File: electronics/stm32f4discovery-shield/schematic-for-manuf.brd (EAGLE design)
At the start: 101.6 x 105.4 mm, 43 parts, among them IC1 MAX3468CPA, IC3 LM340H-12, IC4 LM340H-12, J1 POWER_JACKSLT, Q1 BC548

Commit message: Algumas alteracoes, adicao de anotacoes.
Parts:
- moved I2C3_IMU 5.43 mm to (90.8, 82.7)
- moved AN1 1.27 mm to (10.5, 74.3)
- moved US2 1.27 mm to (10.5, 57.5)
- moved I2C1_ESC 0.64 mm to (90.8, 60.0)
- moved SPI1 0.64 mm to (90.8, 42.9)
- moved US6 0.63 mm to (9.84, 14.9)
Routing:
- net 5V: track 431.6 -> 425.5 mm
- net N$9: track 53.4 -> 48.3 mm
- net SDA2: track 91.1 -> 87.5 mm
- net GND: track 17.8 -> 14.4 mm
- net 3.3V: track 134.9 -> 136.2 mm
- net PA3/USART2_RX: track 28.5 -> 27.2 mm
- net PA2/USART2_TX: track 16.5 -> 17.7 mm
- net N$10: track 8.29 -> 9.49 mm
- net ADC3: track 27.6 -> 26.4 mm
- net ADC1: track 17.6 -> 18.6 mm
- net PB3/SPI1_SCK: track 24.4 -> 23.7 mm
- net SCL1: track 50.1 -> 49.4 mm
- net PC6/USART6_TX: track 68.7 -> 69.3 mm
- net SDA1: track 67.8 -> 68.4 mm
- net PB4/SPI1_MISO: track 23.1 -> 23.7 mm
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
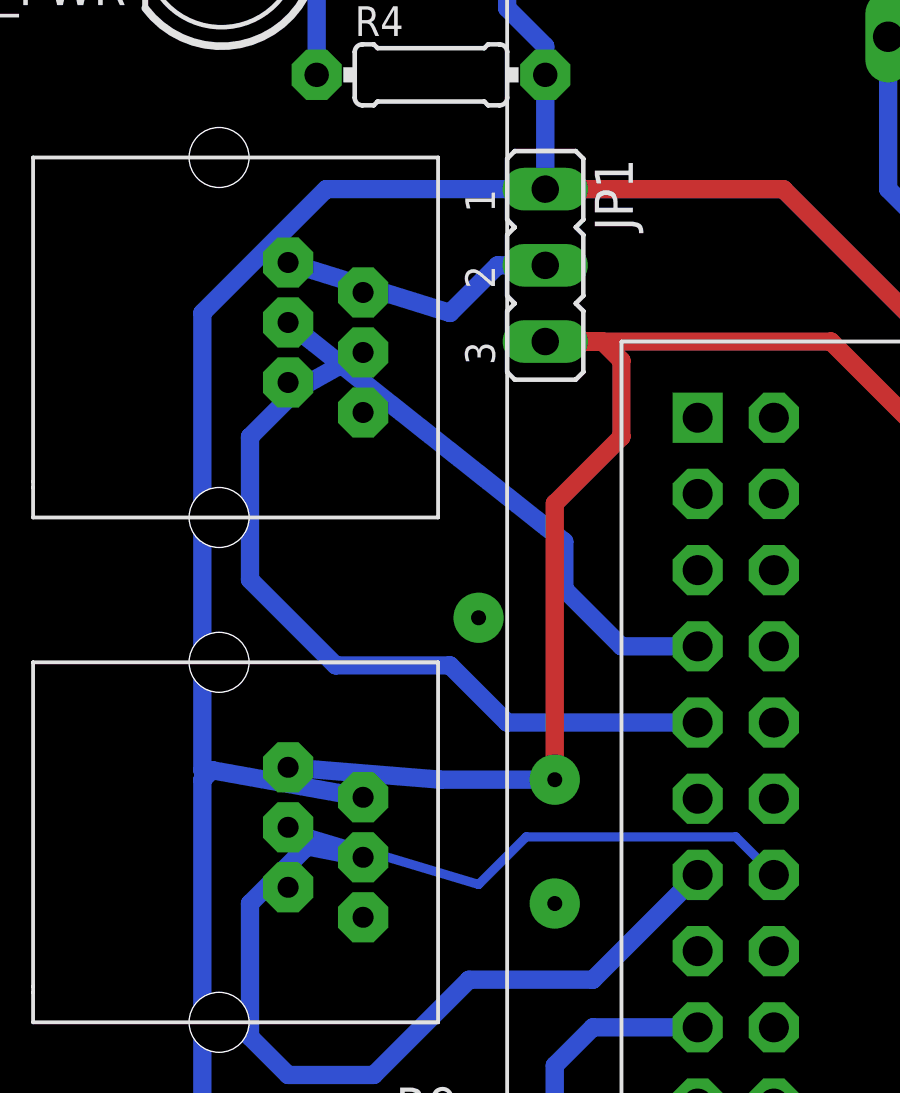
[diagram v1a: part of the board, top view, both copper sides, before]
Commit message: new file:   .gitignore 	modified:   electronics/stm32f4discovery-shield/anotacoes_para_manufatura.txt 	modified:   electronics/stm32f4discovery-shield/schematic-for-manuf.brd
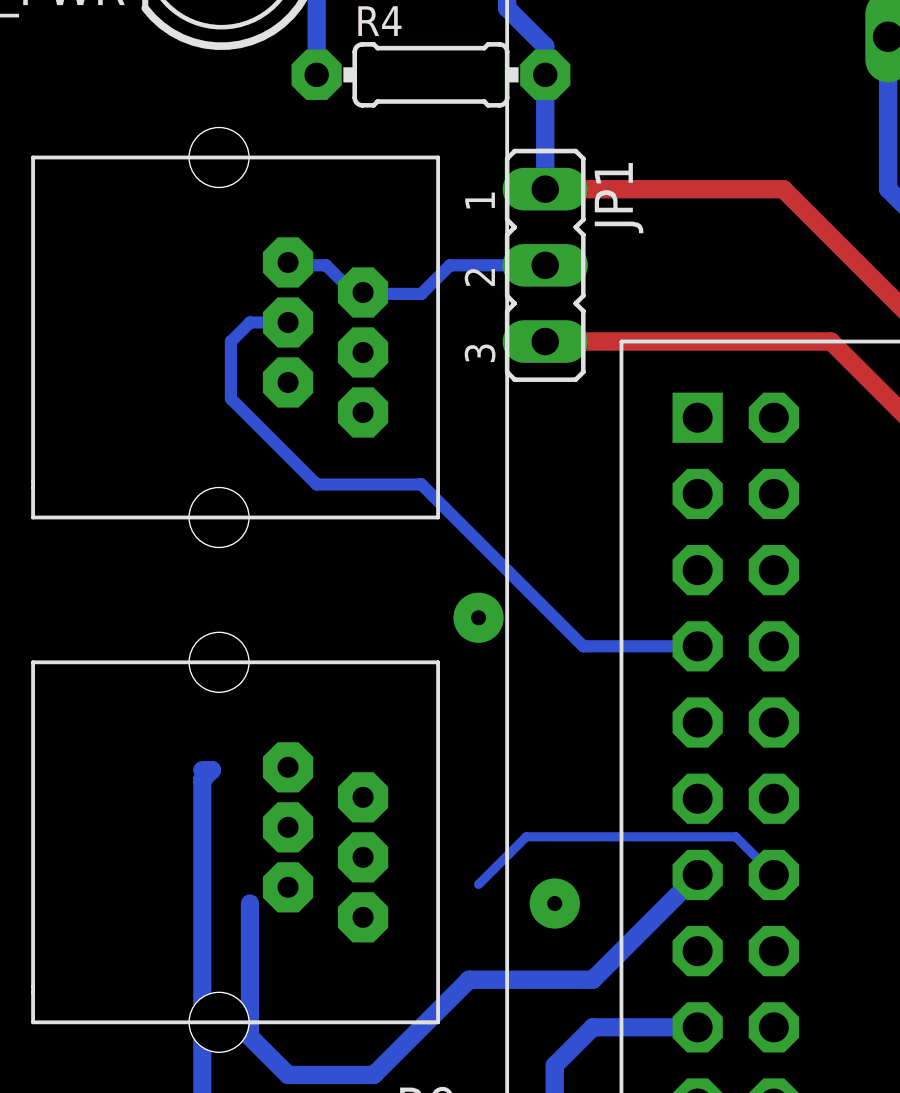
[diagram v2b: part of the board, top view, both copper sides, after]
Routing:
- net 5V: track 425.5 -> 392.0 mm
- net 3.3V: track 136.2 -> 109.2 mm, vias 1 -> 0
- net ADC3: track 26.4 -> 0.00 mm
- net PA2/USART2_TX: track 17.7 -> 11.0 mm
- net PA3/USART2_RX: track 27.2 -> 22.7 mm
- net ADC1: track 18.6 -> 23.0 mm
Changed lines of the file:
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@@
 <?xml version="1.0" encoding="utf-8"?>
 <!DOCTYPE eagle SYSTEM "eagle.dtd">
-<eagle version="6.4">
+<eagle version="6.5.0">
 <drawing>
 <settings>
@@
 <setting verticaltext="up"/>
 </settings>
-<grid distance="25" unitdist="mil" unit="mil" style="lines" multiple="1" display="yes" altdistance="0.025" altunitdist="inch" altunit="inch"/>
+<grid distance="12.5" unitdist="mil" unit="mil" style="lines" multiple="1" display="yes" altdistance="0.025" altunitdist="inch" altunit="inch"/>
 <layers>
 <layer number="1" name="Top" color="4" fill="1" visible="yes" active="yes"/>
@@
 </class>
 </classes>
-<designrules name="default">
+<designrules name="default *">
 <description language="de">&lt;b&gt;EAGLE Design Rules&lt;/b&gt;
 &lt;p&gt;
@@
 <param name="mdSmdStop" value="0mil"/>
 <param name="msWidth" value="10mil"/>
-<param name="msDrill" value="24mil"/>
+<param name="msDrill" value="0.4mm"/>
 <param name="msMicroVia" value="9.99mm"/>
 <param name="msBlindViaRatio" value="0.5"/>
@@
 <wire x1="89.535" y1="56.1975" x2="92.075" y2="56.1975" width="0.6096" layer="16"/>
 <wire x1="88.305" y1="59.0075" x2="89.535" y2="56.1975" width="0.6096" layer="16"/>
-<wire x1="7.62" y1="59.3725" x2="7.62" y2="74.6125" width="0.6096" layer="16"/>
 <wire x1="92.075" y1="56.1975" x2="92.075" y2="51.1175" width="0.6096" layer="16"/>
 <wire x1="92.075" y1="51.1175" x2="92.075" y2="50.8" width="0.6096" layer="16"/>
@@
 <wire x1="94.615" y1="58.7375" x2="92.075" y2="56.1975" width="0.6096" layer="16"/>
 <contactref element="JP1" pad="1"/>
-<wire x1="19.05" y1="78.74" x2="11.7475" y2="78.74" width="0.6096" layer="16"/>
-<wire x1="11.7475" y1="78.74" x2="7.62" y2="74.6125" width="0.6096" layer="16"/>
 <wire x1="17.78" y1="84.7725" x2="19.05" y2="83.5025" width="0.6096" layer="16"/>
 <wire x1="19.05" y1="83.5025" x2="19.05" y2="82.55" width="0.6096" layer="16"/>
@@
 <wire x1="95.5675" y1="13.6525" x2="93.0275" y2="11.1125" width="0.6096" layer="16"/>
 <wire x1="93.0275" y1="11.1125" x2="87.67" y2="13.9225" width="0.6096" layer="16"/>
-<wire x1="12.9775" y1="58.4675" x2="7.9375" y2="59.3725" width="0.6096" layer="16"/>
 <wire x1="7.9375" y1="59.3725" x2="7.62" y2="59.3725" width="0.6096" layer="16"/>
 <wire x1="88.305" y1="81.725" x2="93.345" y2="80.3275" width="0.6096" layer="16"/>
@@
 <wire x1="12.3425" y1="15.9225" x2="13.335" y2="17.4625" width="0.6096" layer="16"/>
 <wire x1="13.335" y1="17.4625" x2="9.8425" y2="16.9225" width="0.6096" layer="16"/>
+<wire x1="12.9775" y1="58.4675" x2="19.05" y2="78.74" width="0" layer="19" extent="16-16"/>
+<wire x1="7.9375" y1="59.3725" x2="12.9775" y2="58.4675" width="0" layer="19" extent="16-16"/>
 </signal>
 <signal name="3.3V">
@@
 <contactref element="JP1" pad="3"/>
 <wire x1="52.3875" y1="58.42" x2="49.8475" y2="60.96" width="0.6096" layer="16"/>
-<wire x1="19.05" y1="73.66" x2="20.955" y2="73.66" width="0.6096" layer="1"/>
-<wire x1="20.955" y1="73.66" x2="21.59" y2="73.025" width="0.6096" layer="1"/>
-<wire x1="21.59" y1="73.025" x2="21.59" y2="70.485" width="0.6096" layer="1"/>
-<wire x1="21.59" y1="70.485" x2="19.3675" y2="68.2625" width="0.6096" layer="1"/>
-<wire x1="19.3675" y1="68.2625" x2="19.3675" y2="59.055" width="0.6096" layer="1"/>
-<via x="19.3675" y="59.055" extent="1-16" drill="0.5" diameter="1.6764" shape="octagon"/>
-<wire x1="19.05" y1="59.3725" x2="19.3675" y2="59.055" width="0.6096" layer="16"/>
-<wire x1="10.4775" y1="59.4675" x2="15.5575" y2="59.055" width="0.6096" layer="16"/>
-<wire x1="15.5575" y1="59.055" x2="19.3675" y2="59.055" width="0.6096" layer="16"/>
 <wire x1="52.3875" y1="58.42" x2="53.975" y2="58.42" width="0.6096" layer="16"/>
 <wire x1="53.975" y1="58.42" x2="69.5325" y2="58.42" width="0.6096" layer="16"/>
@@
 <wire x1="49.8475" y1="67.6275" x2="49.8475" y2="64.77" width="0.6096" layer="16"/>
 <wire x1="49.8475" y1="64.77" x2="49.8475" y2="60.96" width="0.6096" layer="16"/>
+<wire x1="10.4775" y1="59.4675" x2="19.05" y2="73.66" width="0" layer="19" extent="1-1"/>
 </signal>
 <signal name="SDA2">
@@
 <wire x1="25.4" y1="57.15" x2="18.415" y2="57.15" width="0.3048" layer="16"/>
 <wire x1="18.415" y1="57.15" x2="16.8275" y2="55.5625" width="0.3048" layer="16"/>
-<wire x1="16.8275" y1="55.5625" x2="10.4775" y2="57.4675" width="0.3048" layer="16"/>
+<wire x1="10.4775" y1="57.4675" x2="16.8275" y2="55.5625" width="0" layer="19" extent="16-16"/>
 </signal>
 <signal name="PA3/USART2_RX">
@@
 <wire x1="16.51" y1="52.3875" x2="20.6375" y2="52.3875" width="0.6096" layer="16"/>
 <wire x1="20.6375" y1="52.3875" x2="24.13" y2="55.88" width="0.6096" layer="16"/>
-<wire x1="12.9775" y1="56.4675" x2="11.1125" y2="56.8325" width="0.6096" layer="16"/>
-<wire x1="11.1125" y1="56.8325" x2="9.2075" y2="54.9275" width="0.6096" layer="16"/>
+<wire x1="9.2075" y1="54.9275" x2="12.9775" y2="56.4675" width="0" layer="19" extent="16-16"/>
 </signal>
 <signal name="PE11/PWM">
@@
 <contactref element="U$1" pad="P$7"/>
 <contactref element="AN1" pad="P3"/>
-<wire x1="24.13" y1="63.5" x2="21.59" y2="63.5" width="0.6096" layer="16"/>
-<wire x1="21.59" y1="63.5" x2="19.685" y2="65.405" width="0.6096" layer="16"/>
-<wire x1="19.685" y1="65.405" x2="19.685" y2="66.9925" width="0.6096" layer="16"/>
-<wire x1="19.685" y1="66.9925" x2="10.4775" y2="74.295" width="0.6096" layer="16"/>
+<wire x1="24.13" y1="63.5" x2="20.32" y2="63.5" width="0.4064" layer="16"/>
+<wire x1="20.32" y1="63.5" x2="14.9225" y2="68.8975" width="0.4064" layer="16"/>
+<wire x1="14.9225" y1="68.8975" x2="11.43" y2="68.8975" width="0.4064" layer="16"/>
+<wire x1="11.43" y1="68.8975" x2="8.5725" y2="71.755" width="0.4064" layer="16"/>
+<wire x1="8.5725" y1="71.755" x2="8.5725" y2="73.66" width="0.4064" layer="16"/>
+<wire x1="8.5725" y1="73.66" x2="9.2075" y2="74.295" width="0.4064" layer="16"/>
+<wire x1="9.2075" y1="74.295" x2="10.4775" y2="74.295" width="0.4064" layer="16"/>
 </signal>
 <signal name="ADC3">
 <contactref element="U$1" pad="P$9"/>
 <contactref element="AN1" pad="P4"/>
-<wire x1="24.13" y1="60.96" x2="17.78" y2="60.96" width="0.6096" layer="16"/>
-<wire x1="17.78" y1="60.96" x2="15.875" y2="62.865" width="0.6096" layer="16"/>
-<wire x1="15.875" y1="62.865" x2="12.065" y2="62.865" width="0.6096" layer="16"/>
-<wire x1="12.065" y1="62.865" x2="9.2075" y2="65.7225" width="0.6096" layer="16"/>
-<wire x1="9.2075" y1="65.7225" x2="9.2075" y2="70.485" width="0.6096" layer="16"/>
-<wire x1="9.2075" y1="70.485" x2="10.795" y2="72.0725" width="0.6096" layer="16"/>
-<wire x1="10.795" y1="72.0725" x2="12.9775" y2="73.295" width="0.6096" layer="16"/>
+<wire x1="12.9775" y1="73.295" x2="24.13" y2="60.96" width="0" layer="19" extent="1-1"/>
 </signal>
 <signal name="N$10">
 <contactref element="JP1" pad="2"/>
-<wire x1="19.05" y1="76.2" x2="17.4625" y2="76.2" width="0.6096" layer="16"/>
 <contactref element="AN1" pad="P1"/>
-<wire x1="10.4775" y1="76.295" x2="15.875" y2="74.6125" width="0.6096" layer="16"/>
-<wire x1="15.875" y1="74.6125" x2="17.4625" y2="76.2" width="0.6096" layer="16"/>
 <contactref element="AN1" pad="P2"/>
-<wire x1="12.9775" y1="75.295" x2="10.4775" y2="76.295" width="0" layer="19" extent="1-1"/>
+<wire x1="19.05" y1="76.2" x2="15.875" y2="76.2" width="0.4064" layer="16"/>
+<wire x1="15.875" y1="76.2" x2="14.9225" y2="75.2475" width="0.4064" layer="16"/>
+<wire x1="14.9225" y1="75.2475" x2="13.025" y2="75.2475" width="0.4064" layer="16"/>
+<wire x1="13.025" y1="75.2475" x2="12.9775" y2="75.295" width="0.4064" layer="16"/>
+<wire x1="12.9775" y1="75.295" x2="12.6525" y2="75.295" width="0.4064" layer="16"/>
+<wire x1="12.6525" y1="75.295" x2="11.7475" y2="76.2" width="0.4064" layer="16"/>
+<wire x1="11.7475" y1="76.2" x2="10.5725" y2="76.2" width="0.4064" layer="16"/>
+<wire x1="10.5725" y1="76.2" x2="10.4775" y2="76.295" width="0.4064" layer="16"/>
 </signal>
 <signal name="PA7/PWM">

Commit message: Routing principal completo.
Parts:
- moved R11 4.41 mm to (88.3, 52.1)
- moved R2 1.59 mm to (92.4, 29.2)
- moved SRVO1 0.95 mm to (86.7, 101.6)
- moved SRVO2 0.95 mm to (93.7, 101.6)
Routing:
- net PC7/USART6_RX: track 89.3 -> 66.7 mm
- net SCL2: track 100.9 -> 80.3 mm, vias 1 -> 0
- net ADC3: track 0.00 -> 20.1 mm
- net PC9/I2C3_SDA: track 72.3 -> 52.3 mm, vias 1 -> 0
- net 5V: track 392.0 -> 409.1 mm, vias 0 -> 1
- net 3.3V: track 109.2 -> 124.9 mm
- net PA2/USART2_TX: track 11.0 -> 25.0 mm
- net PA3/USART2_RX: track 22.7 -> 11.7 mm
- net SONAR_RX: track 27.9 -> 17.9 mm
- net SRVO2_PWR: track 59.2 -> 67.8 mm
- net PB3/SPI1_SCK: track 23.7 -> 15.3 mm
- net GND: track 14.4 -> 7.67 mm, vias 7 -> 2
- net SCL1: track 49.4 -> 44.9 mm
- net PC6/USART6_TX: track 69.3 -> 73.8 mm
- net PB4/SPI1_MISO: track 23.7 -> 27.7 mm, vias 2 -> 0
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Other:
- board text added: "proVANT board.v3.1"
- board text removed: "proVANT board.v3"

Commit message: Introduzido jumper para servo Dongbu.
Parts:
- added JP2: (no value), jumper:JP2Q
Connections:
- net D+/TX: now also JP2.2
- net D-/RX: now also JP2.4
- net PB6/USART1_TX: now also JP2.1
- net PB7/USART1_RX: now also JP2.3
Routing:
- net PB6/USART1_TX: track 20.2 -> 40.1 mm
- net D+/TX: track 124.6 -> 141.0 mm
- net D-/RX: track 115.4 -> 131.1 mm
- net PB7/USART1_RX: track 37.6 -> 51.3 mm
- net PA8/I2C3_SCL: track 67.5 -> 65.2 mm
- net 5V: track 409.1 -> 410.9 mm
- net PC9/I2C3_SDA: track 52.3 -> 54.0 mm
- net GND: vias 2 -> 0
